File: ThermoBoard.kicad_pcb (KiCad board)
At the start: 4 copper layers, 72.5 x 69 mm, 164 parts, among them J100 Conn_01x05_Pin, J101 Conn_01x03, J103 Screw_Terminal_01x02, J104 USB_C_Receptacle_USB2.0_16P, J200 RJ45_Hanrun_HR911105A_Horizon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, J300 Conn_01x02_Pin, J301 Conn_01x02_Pin, J302 Conn_01x02_Pin, J303 Conn_01x02_Pin, J400 Conn_01x04_Pin, SW100 SW_Push, U100 STM32H563RITx, U101 AP2112K-3.3, U102 USBLC6-2SC6, U200 LAN8742A, U201 USBLC6-4SC6, U300 MAX31856, U301 MAX31856, U302 MAX31856, U303 MAX31856, U400 TJA1042T-3, Y100 X322516MMB4SI, Y200 25MHz

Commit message: I hate everything
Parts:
- removed H200, H201, H202: MountingHole, MountingHole:MountingHole_3.2mm_M3
- removed J300, J301, J302, J303: Conn_01x02_Pin, Connector_PinHeader_2.54mm:PinHeader_1x02_P2.54mm_Vertical
- removed J400: Conn_01x04_Pin, Connector_PinHeader_2.54mm:PinHeader_1x04_P2.54mm_Vertical
- removed R400: 10k, Resistor_SMD:R_0402_1005Metric
- added C118: 22u, Capacitor_SMD:C_0805_2012Metric, F.Cu at (155.8, 112.5)
- added C119: 22u, Capacitor_SMD:C_0805_2012Metric, F.Cu at (155.8, 114.8)
- added C120: 22u, Capacitor_SMD:C_0805_2012Metric, F.Cu at (155.8, 117.0)
- added C121: 22u, Capacitor_SMD:C_0805_2012Metric, F.Cu at (169.6, 90.8)
- added C122: 22u, Capacitor_SMD:C_0805_2012Metric, F.Cu at (167.5, 90.8)
- added C123: 22u, Capacitor_SMD:C_0805_2012Metric, F.Cu at (165.3, 90.8)
- added D103: LED, LED_SMD:LED_0402_1005Metric, F.Cu at (171.6, 103.3)
- added D107: LED, LED_SMD:LED_0402_1005Metric, F.Cu at (150.5, 115.5)
- added D108: LED, LED_SMD:LED_0402_1005Metric, F.Cu at (151.8, 115.5)
- added D109: LED, LED_SMD:LED_0402_1005Metric, F.Cu at (153.0, 115.5)
- added F101: 500mA, Capacitor_SMD:C_0603_1608Metric, F.Cu at (162.5, 106.0)
- added H1: MountingHole, MountingHole:MountingHole_3.2mm_M3, F.Cu at (105.5, 69.2)
- added H2: MountingHole, MountingHole:MountingHole_3.2mm_M3, F.Cu at (169.5, 69.2)
- added H3: MountingHole, MountingHole:MountingHole_3.2mm_M3, F.Cu at (169.5, 129.8)
- added H4: MountingHole, MountingHole:MountingHole_3.2mm_M3, F.Cu at (107.0, 109.0)
- added J102: Conn_01x03, Connector_PinHeader_2.54mm:PinHeader_1x03_P2.54mm_Vertical, F.Cu at (171.8, 122.7)
- added J105: PCC-SMP-K-5, Omega:PCCSMPK5, F.Cu at (107.7, 60.8)
- added J106: PCC-SMP-K-5, Omega:PCCSMPK5, F.Cu at (129.2, 60.8)
- added J107: PCC-SMP-K-5, Omega:PCCSMPK5, F.Cu at (150.7, 60.8)
- added J108: PCC-SMP-K-5, Omega:PCCSMPK5, F.Cu at (172.2, 60.8)
- added JP100: Jumper_2_Bridged, Connector_PinHeader_2.54mm:PinHeader_1x02_P2.54mm_Vertical, F.Cu at (168.4, 103.0)
- added JP400: Jumper_2_Bridged, Connector_PinHeader_2.54mm:PinHeader_1x02_P2.54mm_Vertical, F.Cu at (159.5, 128.0)
- added R104: 330R, Resistor_SMD:R_0402_1005Metric, F.Cu at (171.6, 102.2)
- added R110: 330R, Resistor_SMD:R_0402_1005Metric, F.Cu at (150.5, 117.8)
- added R111: 330R, Resistor_SMD:R_0402_1005Metric, F.Cu at (151.8, 117.8)
- added R112: 330R, Resistor_SMD:R_0402_1005Metric, F.Cu at (153.0, 117.8)
- SW100: footprint Button_Switch_SMD:SW_SPST_B3S-1000 -> Button_Switch_SMD:SW_Push_1P1T_NO_CK_KSC6xxG
- TP101: value +VIN -> TestPoint_Small; footprint TestPoint:TestPoint_Pad_D1.5mm -> TestPoint:TestPoint_Pad_D1.0mm
- TP102: value +3V3 -> TestPoint_Small
- TP103: footprint TestPoint:TestPoint_Pad_D2.0mm -> TestPoint:TestPoint_Pad_D1.5mm
- TP111: value +5V -> TestPoint_Small; footprint TestPoint:TestPoint_Pad_D1.5mm -> TestPoint:TestPoint_Pad_D1.0mm
- moved R313 19.9 mm to (117.3, 90.8), turned to 180 degrees
- moved R106 11.9 mm to (167.0, 116.3)
- moved R214 8.46 mm to (124.6, 124.0), turned to -90 degrees
- moved TP101 4.60 mm to (161.2, 99.8)
- moved C108 4.39 mm to (144.5, 109.8), turned to 0 degrees
- moved C107 3.23 mm to (144.5, 110.8), turned to 0 degrees
- moved SW100 2.94 mm to (117.5, 108.0)
- moved F100 2.42 mm to (160.8, 102.5), turned to -90 degrees
- moved R217 2.12 mm to (110.5, 112.0), turned to 0 degrees
- moved R211 1.65 mm to (126.6, 120.5), turned to 0 degrees
- moved TP103 1.62 mm to (162.0, 95.2)
- moved C403 1.55 mm to (160.9, 123.8)
- moved R215 1.38 mm to (126.6, 123.1), turned to 90 degrees
- moved R213 1.29 mm to (128.3, 119.0)
- moved C208 1.24 mm to (127.6, 123.4), turned to 90 degrees
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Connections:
- net Net-(J300-Pin_2) renamed /Thermocouples/T1_IN-
- net Net-(J301-Pin_2) renamed /Thermocouples/T2_IN-
- net Net-(J302-Pin_2) renamed /Thermocouples/T3_IN-
- net Net-(J303-Pin_2) renamed /Thermocouples/T4_IN-
- C116 pad 2: +VDC -> VBUS
- C403 pad 1: GND -> Net-(JP400-A)
- J103 pad 1: GND -> +VDC
- J103 pad 2: +VDC -> GND
- J104 pad A4: +VDC -> VBUS
- J104 pad A9: +VDC -> VBUS
- J104 pad B4: +VDC -> VBUS
- J104 pad B9: +VDC -> VBUS
- R304 pad 1: Net-(J300-Pin_1) -> /Thermocouples/T1_IN+
- R305 pad 1: Net-(J301-Pin_1) -> /Thermocouples/T2_IN+
- R314 pad 1: Net-(J302-Pin_1) -> /Thermocouples/T3_IN+
- R315 pad 1: Net-(J303-Pin_1) -> /Thermocouples/T4_IN+
- U100 pad 38: unconnected-(U100-PC7-Pad38) -> /Microcontroller/USER_LED_1
- U100 pad 39: unconnected-(U100-PC8-Pad39) -> /Microcontroller/USER_LED_2
- U100 pad 40: unconnected-(U100-PC9-Pad40) -> /Microcontroller/USER_LED_3
- U100 pad 41: unconnected-(U100-PA8-Pad41) -> STDBY
- U102 pad 5: +VDC -> VBUS
- U400 pad 8: Net-(U400-STB) -> STDBY
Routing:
- net +3V3: track 398.8 -> 426.5 mm, vias 31 -> 34
- net STDBY: track 0.00 -> 25.0 mm
- net +5V: track 51.8 -> 30.5 mm
- net /Microcontroller/USER_LED_3: track 0.00 -> 15.7 mm
- net /Microcontroller/USER_LED_2: track 0.00 -> 14.5 mm
- net /Microcontroller/USER_LED_1: track 0.00 -> 13.3 mm
- net +VDC: track 14.2 -> 2.74 mm, vias 2 -> 0
- net Net-(J200-RCT): track 21.0 -> 10.1 mm, vias 0 -> 1
- net /Ethernet/LED2-INTSEL: track 39.8 -> 46.7 mm, vias 2 -> 1
- net NDRDY4: track 60.7 -> 55.5 mm
- net Net-(JP100-B): track 0.00 -> 5.19 mm
- net Net-(J301-Pin_1): track 5.05 -> 0.00 mm
- net Net-(J300-Pin_1): track 4.99 -> 0.00 mm
- net Net-(J303-Pin_1): track 4.93 -> 0.00 mm
- net Net-(J302-Pin_1): track 4.92 -> 0.00 mm
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- added copper zone on F.Cu, net VBUS
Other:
- outline, holes or cut-outs redrawn
- board text added: "+3.3V"
- board text added: "BOOT0"
- board text added: "Close for split termination"
- board text added: "Max 40k per-lead resistance Adjust 0R resistors to match lead resistance"
- board text removed: "+5V ONLY"
- board text removed: "FUSE"

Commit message: First workable layout
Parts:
- added TP112: TestPoint_Small, TestPoint:TestPoint_Pad_D1.0mm, F.Cu at (184.1, 115.1)
- C200, C201: value 5p6 -> 10p
- D105: value 1N4148WT -> MRA4007T3G; footprint Diode_SMD:D_SOD-523 -> Diode_SMD:D_SMA
- SW100: value SW_Push -> K2-1157SP-I4SW-04; footprint Button_Switch_SMD:SW_Push_1P1T_NO_CK_KSC6xxG -> Library:SW-SMD_4P-L6.2-W6.2-P4.50-LS8.6
- moved J105 72.4 mm to (178.5, 76.1)
- moved J108 61.6 mm to (112.5, 75.7)
- moved H4 40.4 mm to (95.5, 147.7)
- moved C116 36.3 mm to (172.5, 139.4), turned to 180 degrees
- moved C202 33.8 mm to (119.7, 141.5), turned to -90 degrees
- moved TP101 31.4 mm to (177.7, 126.5)
- moved J106 31.2 mm to (156.4, 76.0)
- moved U102 30.6 mm to (172.4, 137.0)
- moved F101 30.6 mm to (175.9, 133.4), turned to 0 degrees
- moved R106 30.2 mm to (180.4, 143.4)
- moved J104 30.2 mm to (183.2, 137.3)
- moved J102 30.1 mm to (160.2, 150.4), turned to 90 degrees
- moved R107 29.9 mm to (176.3, 135.6)
- moved R108 29.9 mm to (176.3, 138.6)
- moved JP100 28.4 mm to (178.0, 129.7)
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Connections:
- net Net-(JP100-B) renamed /Microcontroller/USB_FUSE
- J107 pad 1: /Thermocouples/T1_IN- -> /Thermocouples/T3_IN-
- J107 pad 2: /Thermocouples/T1_IN+ -> /Thermocouples/T3_IN+
- SW100 pad 1: GND -> NRST
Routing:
- net SPI_MOSI: track 103.6 -> 134.1 mm
- net SPI_MISO: track 95.8 -> 122.4 mm
- net SPI_SCK: track 93.4 -> 120.0 mm
- net +3V3: track 426.5 -> 405.7 mm, vias 34 -> 31
- net ETH_TX_EN: track 12.1 -> 32.9 mm, vias 0 -> 2
- net ETH_CRS_DV: track 16.4 -> 34.1 mm
- net ETH_RXD0: track 18.6 -> 36.0 mm
- net /Microcontroller/USB_D-: track 17.6 -> 34.2 mm
- net ETH_TXD1: track 19.3 -> 35.8 mm
- net ETH_REF_CLK: track 14.6 -> 30.7 mm
- net /Microcontroller/USB_D+: track 17.6 -> 33.4 mm
- net SPI_CS1: track 29.8 -> 45.2 mm
- net ETH_MDIO: track 20.6 -> 36.0 mm, vias 2 -> 0
- net NFAULT1: track 46.9 -> 61.2 mm
- net SPI_CS3: track 27.4 -> 41.5 mm
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- added copper zone on F.Cu, net /Microcontroller/USB_FUSE
- removed copper zone on F.Cu, net +3.3VA
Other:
- board size 72.5 x 69 mm -> 97 x 96 mm
- board text added: "+3.3VA"
- board text added: "+VDC"
- board text added: "Close jumper for split termination"
- board text added: "FAULT4"
- board text added: "LED3 LED2 LED1"
- board text added: "NFAULT1"
- board text added: "NFAULT2"
- board text added: "NFAULT3"
- board text added: "NRDY1"
- board text added: "NRDY2"
- board text added: "NRDY3"
- board text added: "NRDY4"
- board text added: "PNET"
- board text added: "PWR"
- board text added: "RESET"
- board text added: "SPI_CS1"
- board text added: "SPI_CS2"
- board text added: "SPI_CS3"
- board text added: "SPI_CS4"
- board text added: "USB PWR"
- board text added: "{ "ViaStitching": "0.2", "stitch_zone_0": { "HSpacing": "2.5", "VSpacing": "2.5", "HOffset": "0", "VOffset": "0", "Clearance": ".5", "Randomize": false } }"
- board text removed: "Close for split termination"

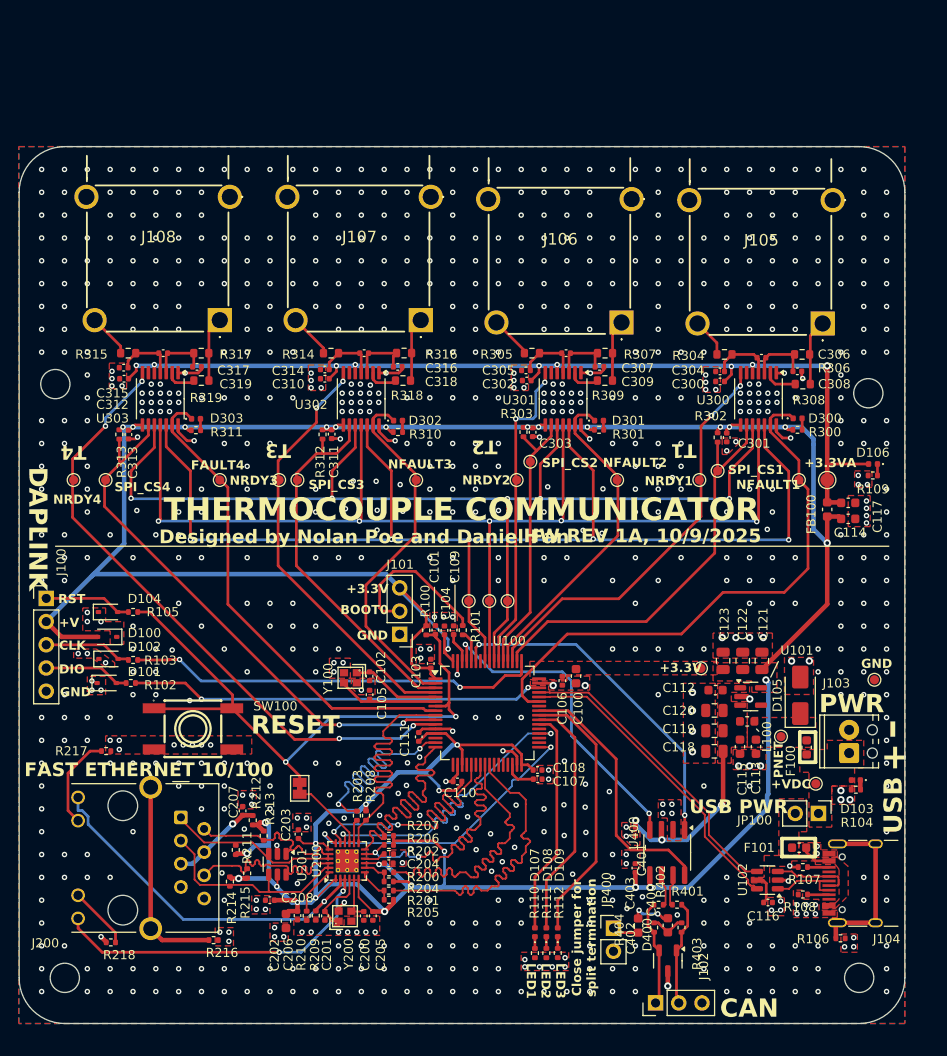
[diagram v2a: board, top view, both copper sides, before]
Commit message: Added pfet for reverse polarity protection, moved power circuitry away from analog parts
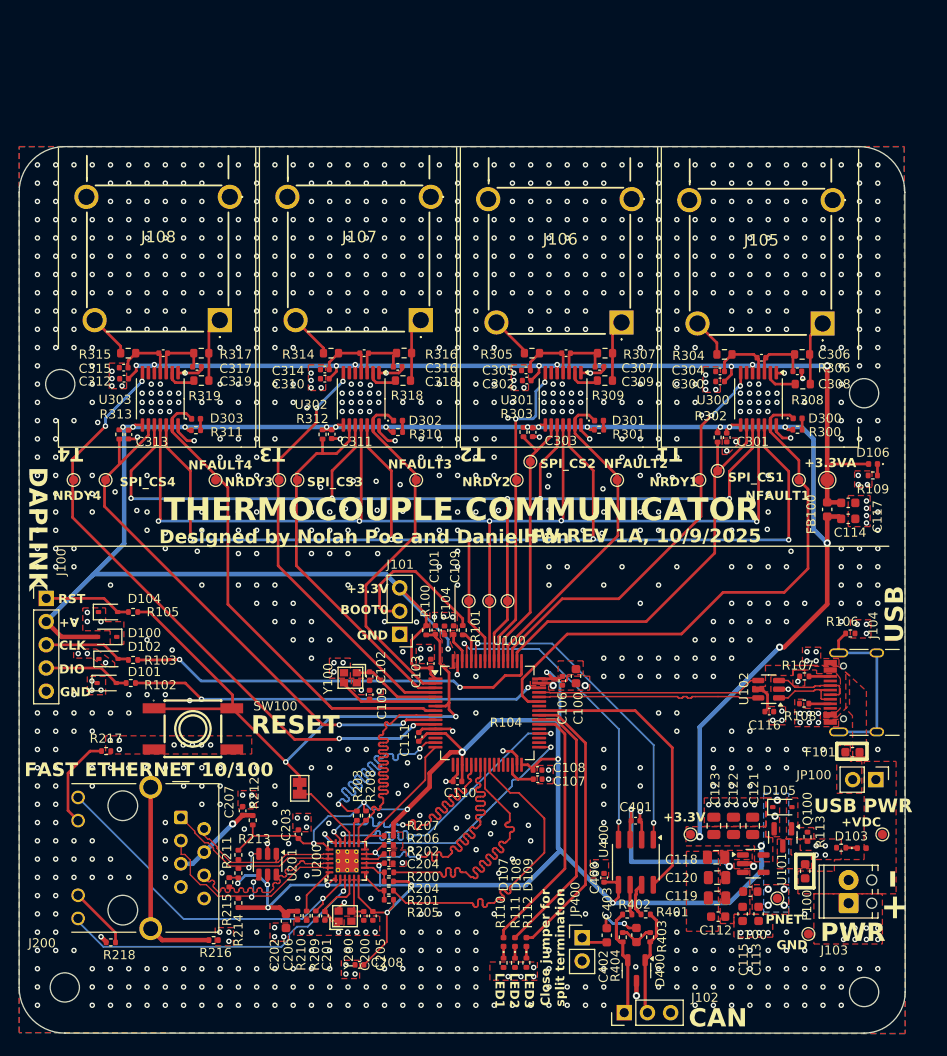
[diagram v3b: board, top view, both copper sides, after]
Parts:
- added Q100: Si2371EDS, Package_TO_SOT_SMD:SOT-23, F.Cu at (174.1, 132.3)
- added R113: 10k, Resistor_SMD:R_0402_1005Metric, F.Cu at (176.8, 132.3)
- D105: value MRA4007T3G -> MM3Z10VT1G; footprint Diode_SMD:D_SMA -> Diode_SMD:D_SOD-323
- moved R106 33.4 mm to (181.5, 110.0)
- moved TP112 28.8 mm to (176.9, 142.9)
- moved C112 24.8 mm to (167.0, 141.0)
- moved U102 20.9 mm to (172.6, 116.1)
- moved C116 20.9 mm to (172.6, 118.5)
- moved J104 20.9 mm to (183.3, 116.5)
- moved R108 20.9 mm to (176.4, 117.7)
- moved R107 20.9 mm to (176.5, 114.7)
- moved L100 18.6 mm to (170.6, 138.3)
- moved C113 18.3 mm to (171.5, 140.7)
- moved C115 18.3 mm to (169.7, 140.7)
- moved C119 18.3 mm to (166.9, 138.9)
- moved C120 18.3 mm to (166.9, 136.7)
- moved U101 18.3 mm to (170.9, 135.2)
- moved TP102 18.2 mm to (164.0, 132.0)
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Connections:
- D105 pad 2: GND -> /Microcontroller/RLOW
- F100 pad 2: /Microcontroller/PNET -> /Microcontroller/FNET
- J103 pad 1: +VDC -> GND
- J103 pad 2: GND -> +VDC
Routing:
- net +3V3: track 405.7 -> 433.5 mm
- net ETH_MDIO: track 36.0 -> 16.7 mm
- net /Microcontroller/USB_D-: track 34.2 -> 24.4 mm
- net /Microcontroller/USB_D+: track 33.4 -> 24.6 mm
- net /Microcontroller/USER_LED_1: track 24.8 -> 28.3 mm
- net VBUS: track 6.76 -> 3.24 mm
- net STDBY: track 28.8 -> 32.1 mm
- net /Ethernet/TX+: track 18.6 -> 21.5 mm, vias 0 -> 2
- net /Microcontroller/USER_LED_2: track 26.8 -> 29.4 mm
- net ETH_CRS_DV: track 34.1 -> 36.6 mm
- net GND: track 44.9 -> 47.2 mm, vias 859 -> 1159
- net /Ethernet/TX-: track 19.3 -> 17.2 mm
- net /Ethernet/LED1-REGOFF: track 36.6 -> 34.8 mm, vias 2 -> 1
- net FDCAN_TX: track 37.8 -> 36.2 mm
- net /Ethernet/RX+: track 23.3 -> 24.7 mm, vias 0 -> 2
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- added copper zone on F.Cu, net /Microcontroller/FNET
- added copper zone on B.Cu, net /Microcontroller/PNET
- added copper zone on F.Cu, net /Microcontroller/RLOW
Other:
- board size 97 x 96 mm -> 97 x 97 mm
- board text added: "NFAULT4"
- board text added: "{ "ViaStitching": "0.2", "stitch_zone_0": { "HSpacing": "2", "VSpacing": "2", "HOffset": "0", "VOffset": "0", "Clearance": ".5", "Randomize": false } }"
- board text removed: "FAULT4"

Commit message: Apply Daniel's suggestions
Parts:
- moved C208 13.3 mm to (115.8, 140.5), turned to -90 degrees
- moved H4 0.70 mm to (95.0, 149.2)
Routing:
- net +3V3: track 433.5 -> 426.7 mm
- net GND: vias 1159 -> 1117
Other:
- outline, holes or cut-outs redrawn
- board text added: "CAN- CAN+ GND"
- board text added: "ETH NRST"
- board text added: "PC9 PC8 PC7"
- board text added: "{ "ViaStitching": "0.2", "stitch_zone_0": { "HSpacing": "2.", "VSpacing": "2", "HOffset": "0", "VOffset": "0", "Clearance": ".5", "Randomize": false } }"
- board text removed: "CAN+"
- board text removed: "CAN-"
- board text removed: "LED3 LED2 LED1"
